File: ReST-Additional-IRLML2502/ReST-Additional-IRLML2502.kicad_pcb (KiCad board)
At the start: 2 copper layers, 23.8 x 27.9 mm, 30 parts, among them P1 CONN_02X07, P2 CONN_01X08, P3 SCREW_01X04, P4 SCREW_01X04, Q1 IRLML2502, Q2 IRLML2502, Q3 IRLML2502, Q4 IRLML2502

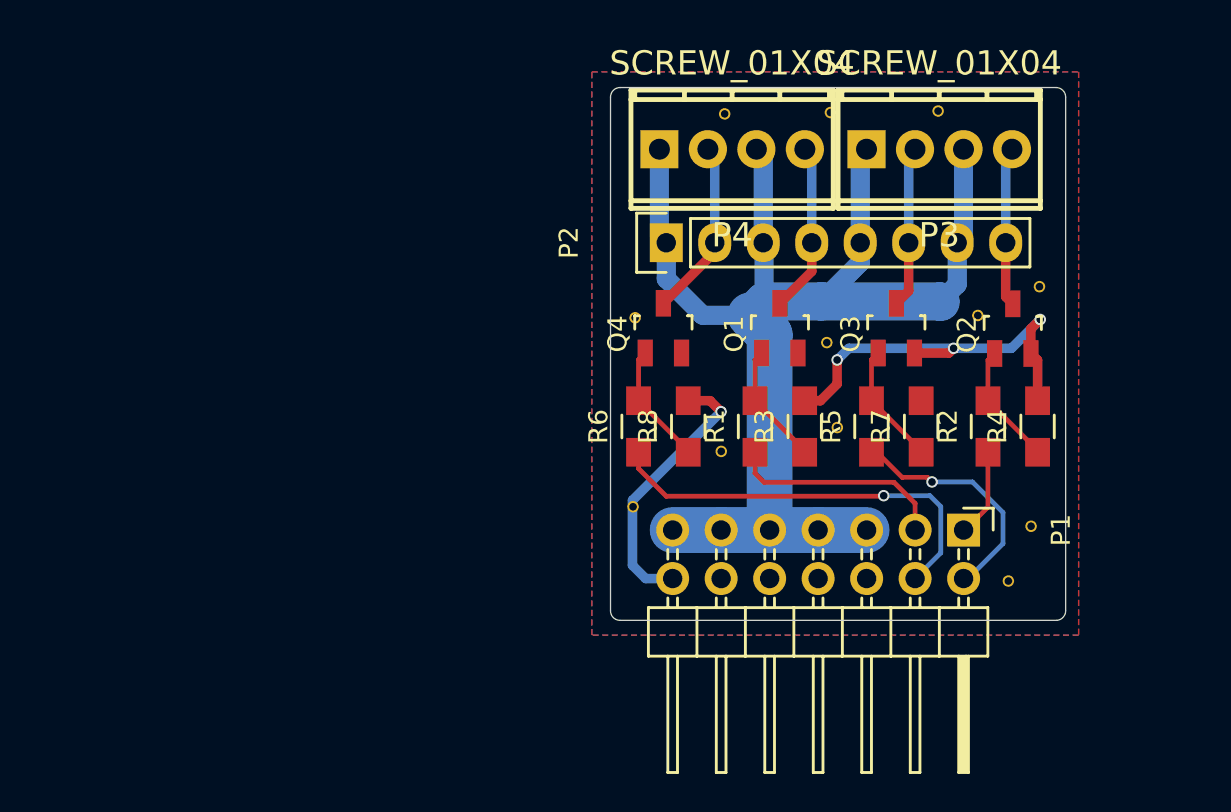
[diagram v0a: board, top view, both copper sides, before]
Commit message: Added BOM for all Items + suggested Links
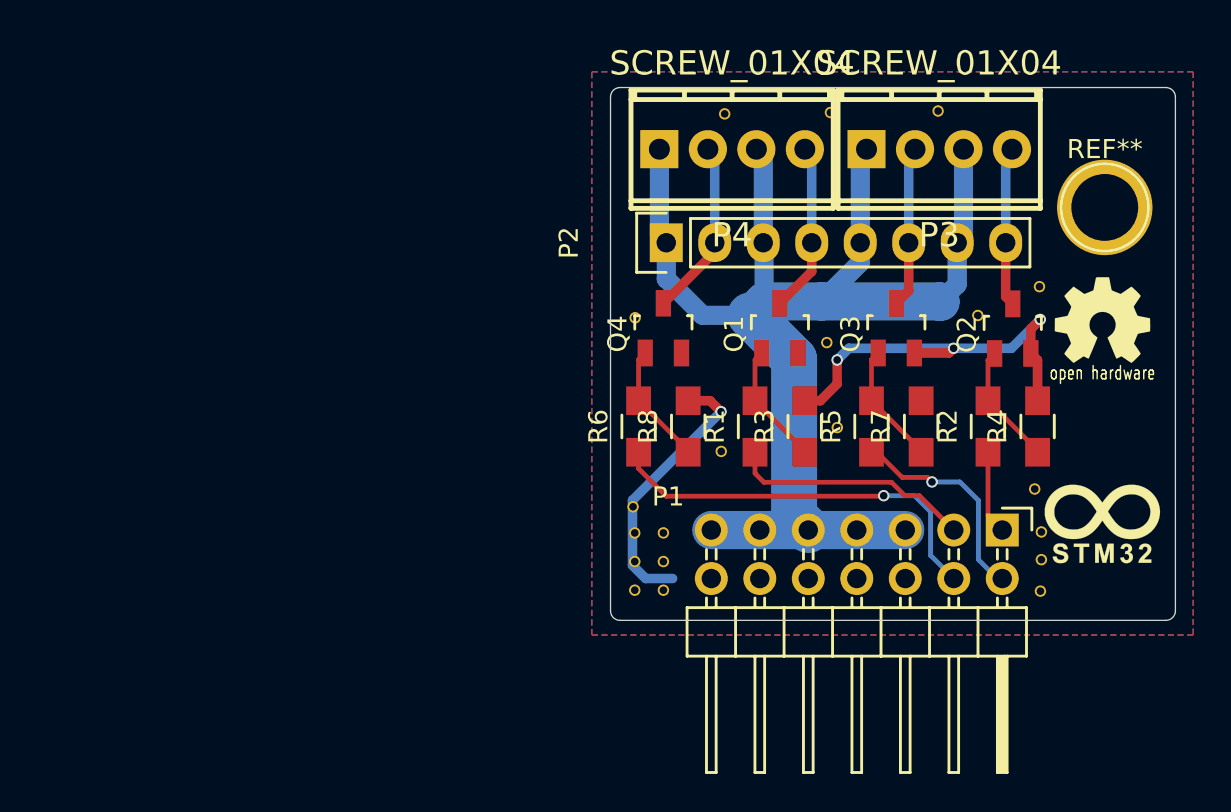
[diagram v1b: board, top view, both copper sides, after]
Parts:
- added REF**: VIA-0.6mm, ReST-Library:VIA-0.6mm, F.Cu at (181.1, 106.1)
- added REF**: 1pin, Connect:1pin, F.Cu at (184.4, 89.1)
- added REF**: VIA-0.6mm, ReST-Library:VIA-0.6mm, F.Cu at (181.1, 107.5)
- added REF**111: VIA-0.6mm, ReST-Library:VIA-0.6mm, F.Cu at (159.8, 106.2)
- added REF**112: VIA-0.6mm, ReST-Library:VIA-0.6mm, F.Cu at (159.8, 107.7)
- added REF**113: VIA-0.6mm, ReST-Library:VIA-0.6mm, F.Cu at (159.8, 109.2)
- added REF**121: VIA-0.6mm, ReST-Library:VIA-0.6mm, F.Cu at (161.2, 106.2)
- added REF**122: VIA-0.6mm, ReST-Library:VIA-0.6mm, F.Cu at (161.2, 107.7)
- added REF**123: VIA-0.6mm, ReST-Library:VIA-0.6mm, F.Cu at (161.2, 109.2)
- G*** (x2): moved to F.Cu
- moved G*** 19.5 mm to (184.2, 95.0), turned to 0 degrees
- moved G*** 11.5 mm to (184.2, 105.8), turned to 0 degrees
- moved P1 2.03 mm to (179.0, 106.0)
- moved REF** 1.96 mm to (180.7, 103.8)
- moved REF** 1.76 mm to (181.0, 109.2)
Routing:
- net /PWM-ADD1: track 12.8 -> 11.4 mm
- net /PWM-ADD2: track 11.5 -> 12.7 mm
- net +12V: track 69.8 -> 70.9 mm
- net /PWM-ADD3: track 21.9 -> 21.1 mm
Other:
- board size 23.8 x 27.9 mm -> 29.6 x 27.9 mm

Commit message: Finished PCB design, notations and silkscreen
gonna work to finish a combined design for cheaper pcb cost and put
everything i need into the bom
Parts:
- removed REF**: VIA-0.6mm, ReST-Library:VIA-0.6mm
- added ?: , ReST-Library:VIA-0.6mm, F.Cu at (164.0, 93.6)
- added ?: , ReST-Library:VIA-0.6mm, F.Cu at (162.7, 88.0)
- added ?: , ReST-Library:VIA-0.6mm, F.Cu at (165.1, 88.1)
- added ?: , ReST-Library:VIA-0.6mm, F.Cu at (167.8, 88.1)
- added ?: , ReST-Library:VIA-0.6mm, F.Cu at (170.2, 88.1)
- added ?: , ReST-Library:VIA-0.6mm, F.Cu at (172.9, 88.1)
- added ?: , ReST-Library:VIA-0.6mm, F.Cu at (175.5, 88.0)
- added ?: , ReST-Library:VIA-0.6mm, F.Cu at (178.4, 88.0)
- ?: renamed from REF**113; value VIA-0.6mm -> (none)
- ?: renamed from REF**122; value VIA-0.6mm -> (none)
- ?: renamed from REF**112; value VIA-0.6mm -> (none)
- ?: renamed from REF**121; value VIA-0.6mm -> (none)
- ?: renamed from REF**111; value VIA-0.6mm -> (none)
- ? (x13): renamed from REF**; value VIA-0.6mm -> (none)
- ? (x2): renamed from G***; value LOGO -> (none)
- ?: renamed from REF**; value 1pin -> (none)
- ?: renamed from REF**123; value VIA-0.6mm -> (none)
- P1: value CONN_02X07 -> (none); footprint Pin_Headers:Pin_Header_Angled_2x07 -> ReST-Library:Pin_Header_Angled_2x07
- P2: value CONN_01X08 -> (none)
- P3, P4: value SCREW_01X04 -> (none)
- Q1, Q2, Q3, Q4: value IRLML2502 -> (none)
- R1, R2, R5, R6: value 27R -> (none)
- R3, R4, R7, R8: value 100K -> (none)
- moved ? 6.70 mm to (184.4, 101.8)
- moved ? 6.52 mm to (186.0, 101.8)
- moved ? 6.18 mm to (185.8, 105.3)
- moved ? 2.55 mm to (182.8, 105.3)
- moved ? 2.06 mm to (184.9, 97.0)
- moved ? 0.45 mm to (159.3, 105.1)
- moved ? 0.16 mm to (184.3, 105.9)
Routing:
- net +12V: track 70.9 -> 73.5 mm
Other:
- board text added: "Additional Module - IRLML2502 Rev. A @maker_berry"
- board text removed: "Additional Module - IRLML2502 PCB by Straw"

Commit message: Final release
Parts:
- moved P3 0.10 mm to (175.7, 86.2)
- moved P4 0.10 mm to (164.8, 86.2)
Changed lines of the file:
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@@
     (links 71)
     (no_connects 0)
-    (area 157.175 79.82512 189.000001 119.425001)
+    (area 157.175 79.925 189.000001 113.625)
     (thickness 1.6)
     (drawings 9)
@@
     (visible_elements 7FFFFFFF)
     (pcbplotparams
-      (layerselection 0x00030_80000001)
-      (usegerberextensions false)
+      (layerselection 0x010f0_80000001)
+      (usegerberextensions true)
       (excludeedgelayer true)
       (linewidth 0.100000)
@@
       (outputformat 1)
       (mirror false)
-      (drillshape 1)
+      (drillshape 0)
       (scaleselection 1)
-      (outputdirectory ""))
+      (outputdirectory ../Gerber/Additional/))
   )
   (net 0 "")
@@
   )
   (module 2:mpt_0,5%2f4-2,54 (layer F.Cu)
-    (at 175.7 86.05 180)
+    (at 175.7 86.15 180)
     (descr "4-way 2.54mm pitch terminal block, Phoenix MPT series")
     (fp_text reference P3 (at -6.7 1.125 270) (layer F.SilkS)
@@
   )
   (module 2:mpt_0,5%2f4-2,54 (layer F.Cu)
-    (at 164.85 86.05 180)
+    (at 164.85 86.15 180)
     (descr "4-way 2.54mm pitch terminal block, Phoenix MPT series")
     (fp_text reference P4 (at 3.875 -1.925 180) (layer F.SilkS)
@@
     (descr "Through hole pin header")
     (tags "pin header")
-    (fp_text reference P1 (at -1.75 17.5 360) (layer F.SilkS)
-      (effects (font (size 1 1) (thickness 0.15)))
-    )
+    (fp_text reference P1 (at 0.05 18 450) (layer F.SilkS)
+      (effects (font (size 1 1) (thickness 0.15)))
+    )

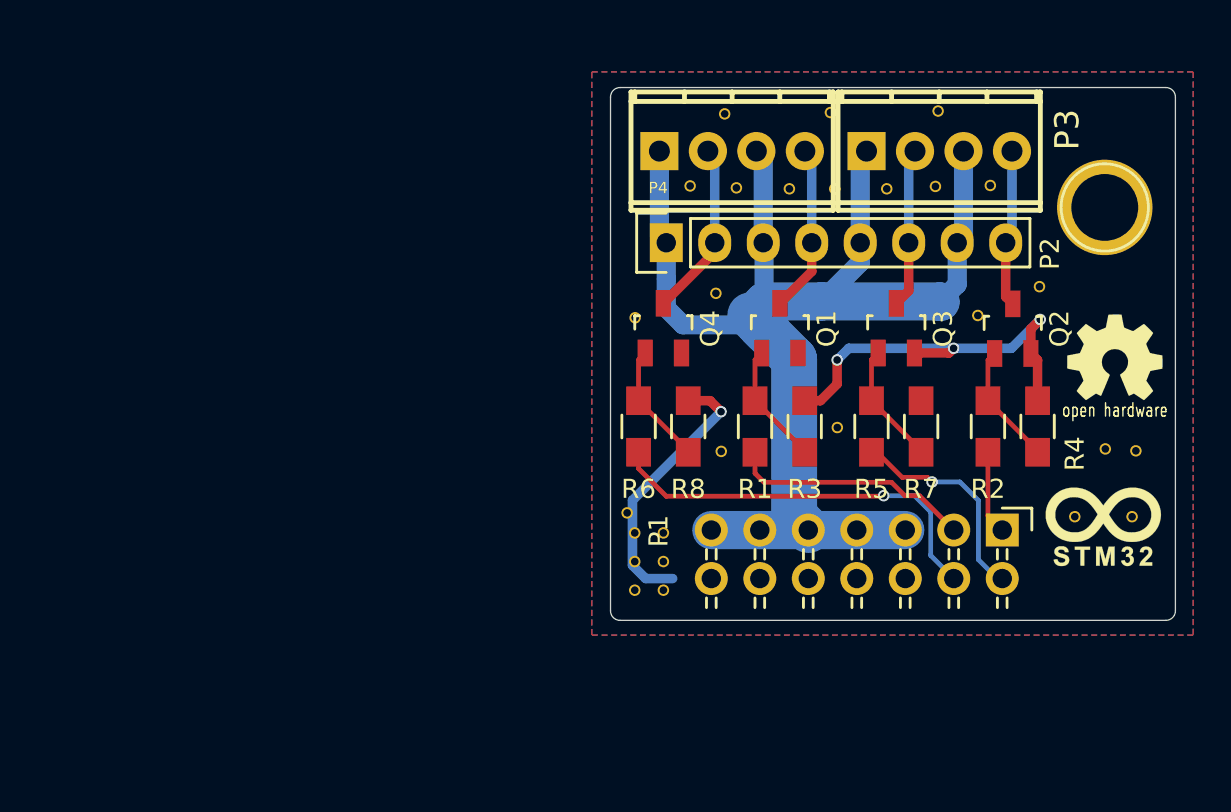
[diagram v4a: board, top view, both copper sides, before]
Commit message: Reworked Modules to sit ontop of the mainboard
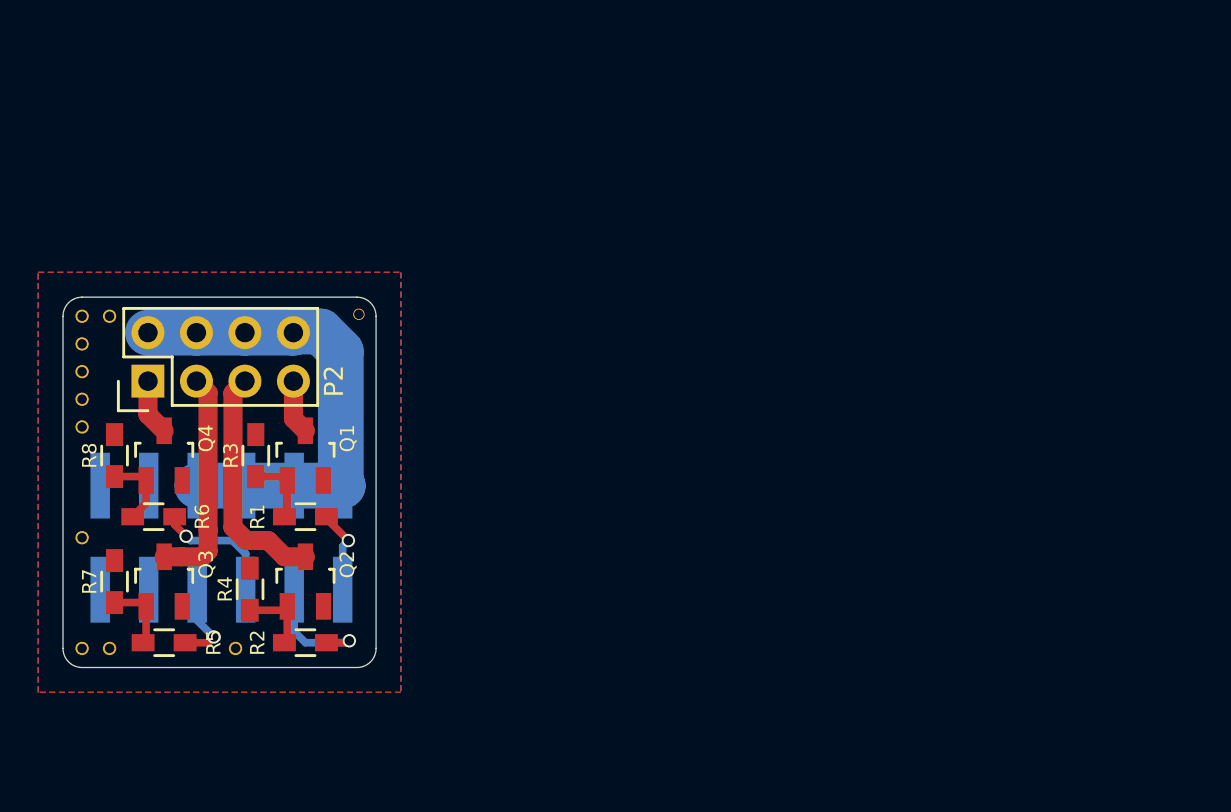
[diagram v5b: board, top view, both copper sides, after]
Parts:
- removed the ? at (164.0, 93.6)
- removed the ? at (159.8, 109.2)
- removed the ? at (161.2, 107.7)
- removed the ? at (159.8, 107.7)
- removed the ? at (161.2, 106.2)
- removed the ? at (159.8, 106.2)
- removed the ? at (186.0, 101.8)
- removed the ? at (184.4, 101.8)
- removed the ? at (175.6, 84.0)
- removed the ? at (170.0, 84.1)
- removed the ? at (164.5, 84.2)
- removed the ? at (162.7, 88.0)
- removed the ? at (182.8, 105.3)
- removed the ? at (185.8, 105.3)
- removed the ? at (159.8, 94.9)
- removed the ? at (164.3, 101.9)
- removed the ? at (170.4, 100.6)
- removed the ? at (177.7, 94.8)
- removed the ? at (180.9, 93.2)
- removed the ? at (159.3, 105.1)
- removed the ? at (184.9, 97.0)
- removed the ? at (184.3, 105.9)
- removed the ? at (165.1, 88.1)
- removed the ? at (184.4, 89.1)
- removed the ? at (167.8, 88.1)
- removed the ? at (170.2, 88.1)
- removed the ? at (172.9, 88.1)
- removed the ? at (175.5, 88.0)
- removed the ? at (178.4, 88.0)
- removed the ? at (161.2, 109.2)
- removed P3, P4: , 2:mpt_0,5%2f4-2,54
- added ?: 1pin, ReST-Library:1pin, F.Cu at (138.8, 112.2)
- added ?: 1pin, ReST-Library:1pin, F.Cu at (132.2, 94.8)
- added ?: 1pin, ReST-Library:1pin, F.Cu at (130.8, 94.8)
- added ?: 1pin, ReST-Library:1pin, F.Cu at (132.2, 112.2)
- added ?: 1pin, ReST-Library:1pin, F.Cu at (130.8, 112.2)
- added ?: 1pin, ReST-Library:1pin, F.Cu at (130.8, 106.4)
- added ?: 1pin, ReST-Library:1pin, F.Cu at (130.8, 100.6)
- added ?: 1pin, ReST-Library:1pin, F.Cu at (130.8, 99.2)
- added ?: 1pin, ReST-Library:1pin, F.Cu at (130.8, 97.7)
- added ?: 1pin, ReST-Library:1pin, F.Cu at (130.8, 96.2)
- added ?: 1pin, ReST-Library:1pin, F.Cu at (145.3, 94.7)
- P1: value (none) -> CONN_02X06; footprint ReST-Library:Pin_Header_Angled_2x07 -> ReST-Library:bb02-hp12; moved to B.Cu
- P2: value (none) -> CONN_02X04; footprint Pin_Headers:Pin_Header_Straight_1x08 -> Pin_Headers:Pin_Header_Straight_2x04
- Q1, Q2, Q3, Q4: value (none) -> IRLML2502
- R1, R2, R5, R6: value (none) -> 27R; footprint Resistors_SMD:R_0805_HandSoldering -> Resistors_SMD:R_0603_HandSoldering
- R3, R4, R7, R8: value (none) -> 100K; footprint Resistors_SMD:R_0805_HandSoldering -> Resistors_SMD:R_0603_HandSoldering
- moved R7 43.0 mm to (132.5, 108.7)
- moved R4 42.1 mm to (139.6, 109.1)
- moved P1 40.9 mm to (138.1, 106.4), turned to 180 degrees
- moved Q3 40.6 mm to (135.1, 108.7)
- moved Q2 39.3 mm to (142.5, 108.7)
- moved R5 38.7 mm to (135.1, 111.9), turned to 180 degrees
- moved R2 37.5 mm to (142.5, 111.9), turned to 180 degrees
- moved R8 30.1 mm to (132.5, 102.1)
- moved R3 28.8 mm to (139.9, 102.1)
- moved P2 28.1 mm to (134.2, 98.2)
- moved Q4 27.0 mm to (135.1, 102.1)
- moved R6 25.8 mm to (134.6, 105.3), turned to 180 degrees
- moved Q1 25.7 mm to (142.5, 102.1)
- moved R1 24.0 mm to (142.5, 105.3), turned to 180 degrees
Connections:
- P1 pad 1: /PWM-ADD0 -> /PWM-ADD2
- P1 pad 11: +12V -> GND
- P1 pad 2: /PWM-ADD1 -> +12V
- P1 pad 3: /PWM-ADD2 -> /PWM-ADD0
- P1 pad 4: /PWM-ADD3 -> +12V
- P1 pad 5: +12V -> /PWM-ADD3
- P1 pad 6: GND -> +12V
- P1 pad 7: +12V -> /PWM-ADD1
- P1 pad 8: GND -> +12V
- P1 pad 9: +12V -> GND
- P2 pad 1: +12V -> /PWM-OUT3
- P2 pad 2: /PWM-OUT3 -> +12V
- P2 pad 3: +12V -> /PWM-OUT2
- P2 pad 4: /PWM-OUT0 -> +12V
- P2 pad 5: +12V -> /PWM-OUT1
- P2 pad 6: /PWM-OUT2 -> +12V
- P2 pad 7: +12V -> /PWM-OUT0
- P2 pad 8: /PWM-OUT1 -> +12V
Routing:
- net +12V: track 73.5 -> 25.2 mm
- net GND: track 35.9 -> 0.00 mm, vias 4 -> 0
- net /PWM-ADD3: track 21.1 -> 8.01 mm
- net /PWM-ADD2: track 12.7 -> 4.43 mm, vias 0 -> 1
- net /PWM-ADD1: track 11.4 -> 4.46 mm
- net /PWM-OUT3: track 9.34 -> 2.95 mm
- net /PWM-OUT0: track 8.92 -> 2.86 mm
- net /PWM-OUT1: track 8.39 -> 12.4 mm
- net /PWM-OUT2: track 8.48 -> 11.6 mm
- net Net-(Q1-Pad1): track 6.42 -> 3.69 mm
- net Net-(Q3-Pad1): track 6.42 -> 3.69 mm
- net Net-(Q4-Pad1): track 6.42 -> 3.92 mm
- net Net-(Q2-Pad1): track 6.40 -> 3.99 mm
- net /PWM-ADD0: track 4.39 -> 6.60 mm, vias 0 -> 1
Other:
- board size 29.6 x 27.9 mm -> 16.4 x 19.4 mm
- net class Default: via_dia 0.6 -> 0.7; via_drill 0.4 -> 0.5
- board text removed: "Additional Module - IRLML2502 Rev. A @maker_berry"

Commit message: Mainboard structure made and most modules finished
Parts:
- removed the ? at (138.8, 112.2)
- removed the ? at (132.2, 94.8)
- removed the ? at (132.2, 112.2)
- removed the ? at (130.8, 99.2)
- removed the ? at (130.8, 97.7)
- removed the ? at (130.8, 96.2)
- removed the ? at (145.3, 94.7)
- added ?: , ReST-Library:1pin, F.Cu at (130.8, 104.1)
- added ?: , ReST-Library:1pin, F.Cu at (130.8, 98.3)
- added ?: , ReST-Library:1pin, F.Cu at (130.8, 97.1)
- added ?: , ReST-Library:1pin, F.Cu at (130.8, 96.0)
- added ?: , ReST-Library:1pin, F.Cu at (130.8, 108.7)
- added ?: , ReST-Library:1pin, F.Cu at (139.2, 112.2)
- added ?: , ReST-Library:1pin, F.Cu at (145.2, 94.8)
- added ?: , ReST-Library:1pin, F.Cu at (132.0, 94.8)
- added ?: , ReST-Library:1pin, F.Cu at (130.8, 99.4)
- ? (x4): value 1pin -> (none)
- P1: value CONN_02X06 -> (none)
- P2: value CONN_02X04 -> (none)
- Q1, Q2, Q3, Q4: value IRLML2502 -> (none)
- R1, R2, R5, R6: value 27R -> (none)
- R3, R4, R7, R8: value 100K -> (none)
